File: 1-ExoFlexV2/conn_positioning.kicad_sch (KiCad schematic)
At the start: 39 parts, among them J46 POS_LC1, J47 POS_LC2, J48 POS_LC3, J49 1751099, J50 1751099, J51 1751099, J52 1751112, J53 1751112, J54 1751112, J55 200k, J56 200k, J57 200k, J58 5,1k, J59 5,1k, J60 5,1k

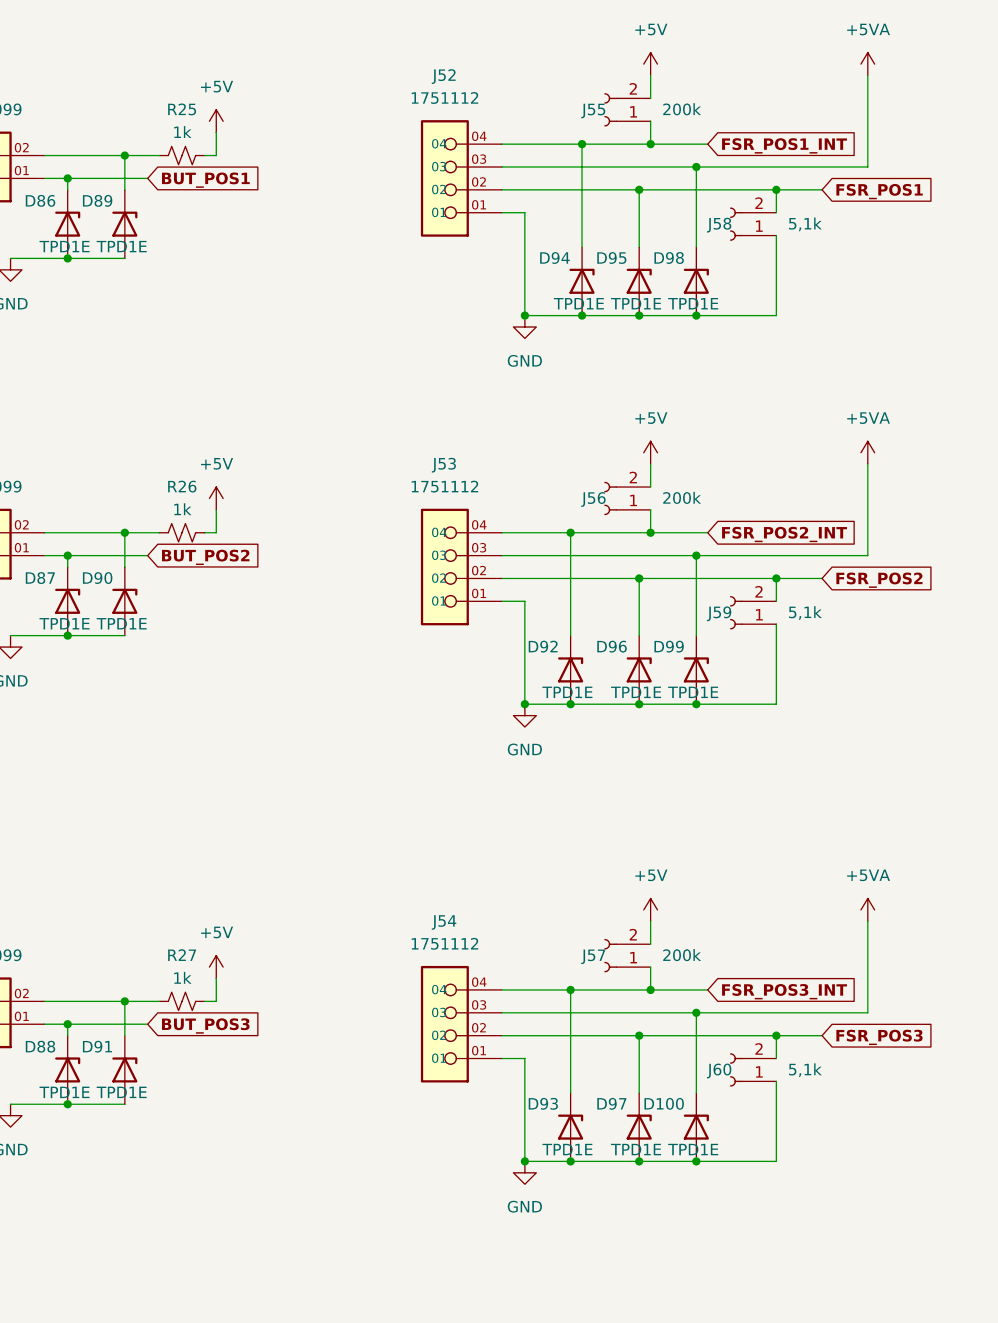
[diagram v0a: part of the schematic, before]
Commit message: Trimmer et jumper
-Changement de symbole de jumper
-Ajout des des trimmer aux endroits nécessaires
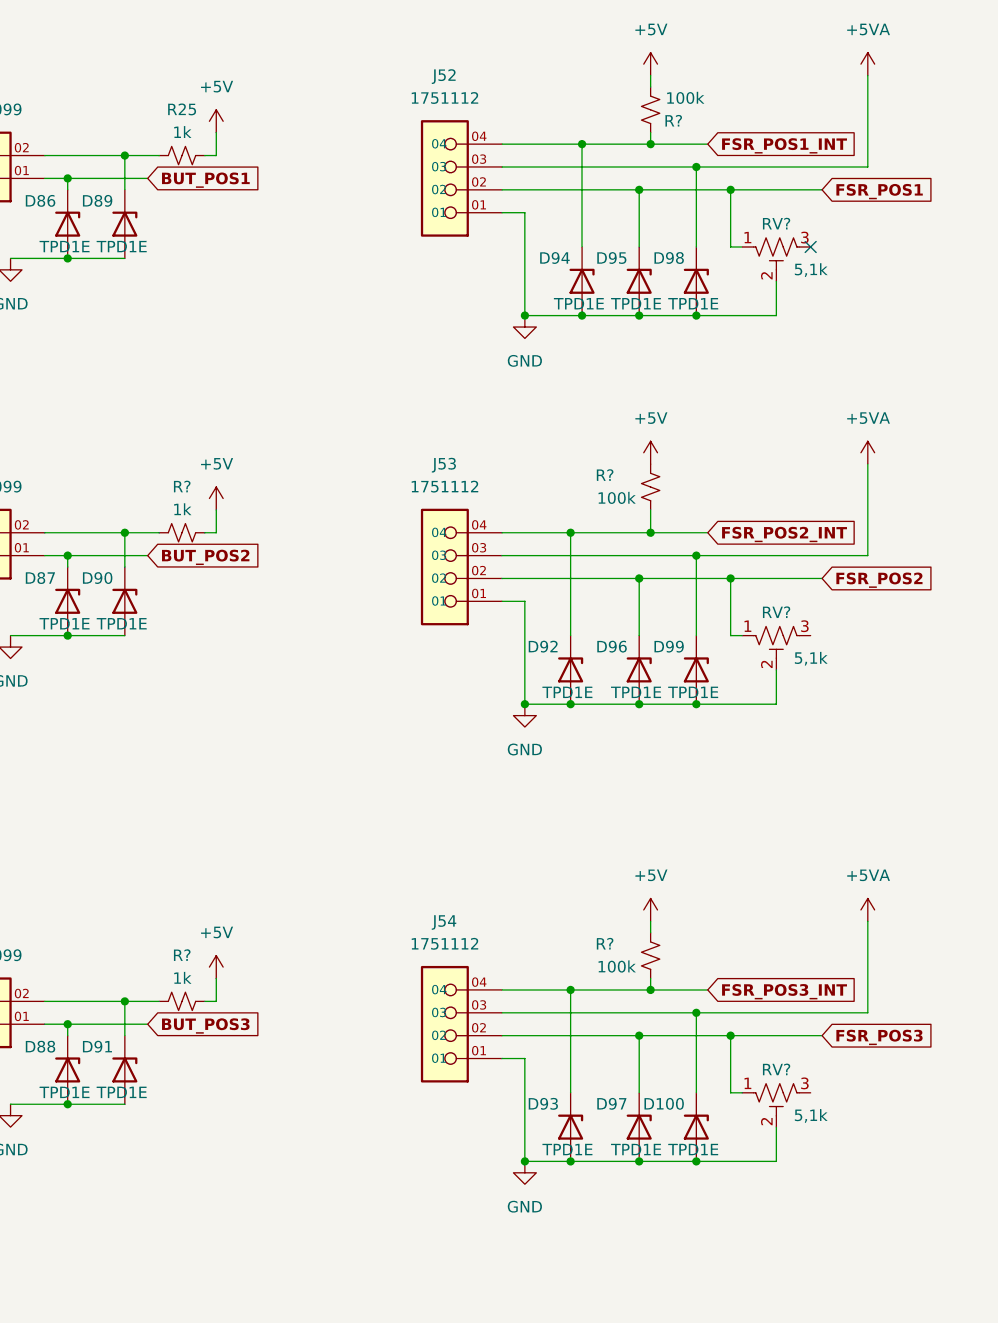
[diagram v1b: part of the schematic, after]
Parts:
- removed J55, J56, J57: 200k, Connector_PinHeader_2.54mm:PinHeader_1x02_P2.54mm_Vertical, symbol Connector:Conn_01x02_Female
- removed J58, J59, J60: 5,1k, Connector_PinHeader_2.54mm:PinHeader_1x02_P2.54mm_Vertical, symbol Connector:Conn_01x02_Female
- removed R26, R27: 1k, Resistor_SMD:R_0603_1608Metric, symbol Device:R_Small_US
- added R? (x2): 1k, Resistor_SMD:R_0805_2012Metric, symbol Device:R_Small_US
- added R? (x3): 100k, Resistor_SMD:R_0805_2012Metric, symbol Device:R_Small_US
- added RV? (x3): 5,1k, FootPrint:TRIM_3362P-1-102LF, symbol Device:R_Potentiometer_Trim_US
- R25: footprint Resistor_SMD:R_0603_1608Metric -> Resistor_SMD:R_0805_2012Metric
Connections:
- net +5V: now also R?.1, R?.1, R?.1, R?.2, R?.2
- net FSR_POS1: now also RV?.1
- net FSR_POS1_INT: now also R?.2
- net FSR_POS2: now also RV?.1
- net FSR_POS2_INT: now also R?.2
- net FSR_POS3: now also RV?.1
- net FSR_POS3_INT: now also R?.2
- net GND: now also RV?.2, RV?.2, RV?.2
- net at D91.1 (K), J51.02: now also R?.1
- net at D90.1 (K), J50.02: now also R?.1
- no-connect marks 0 -> 1

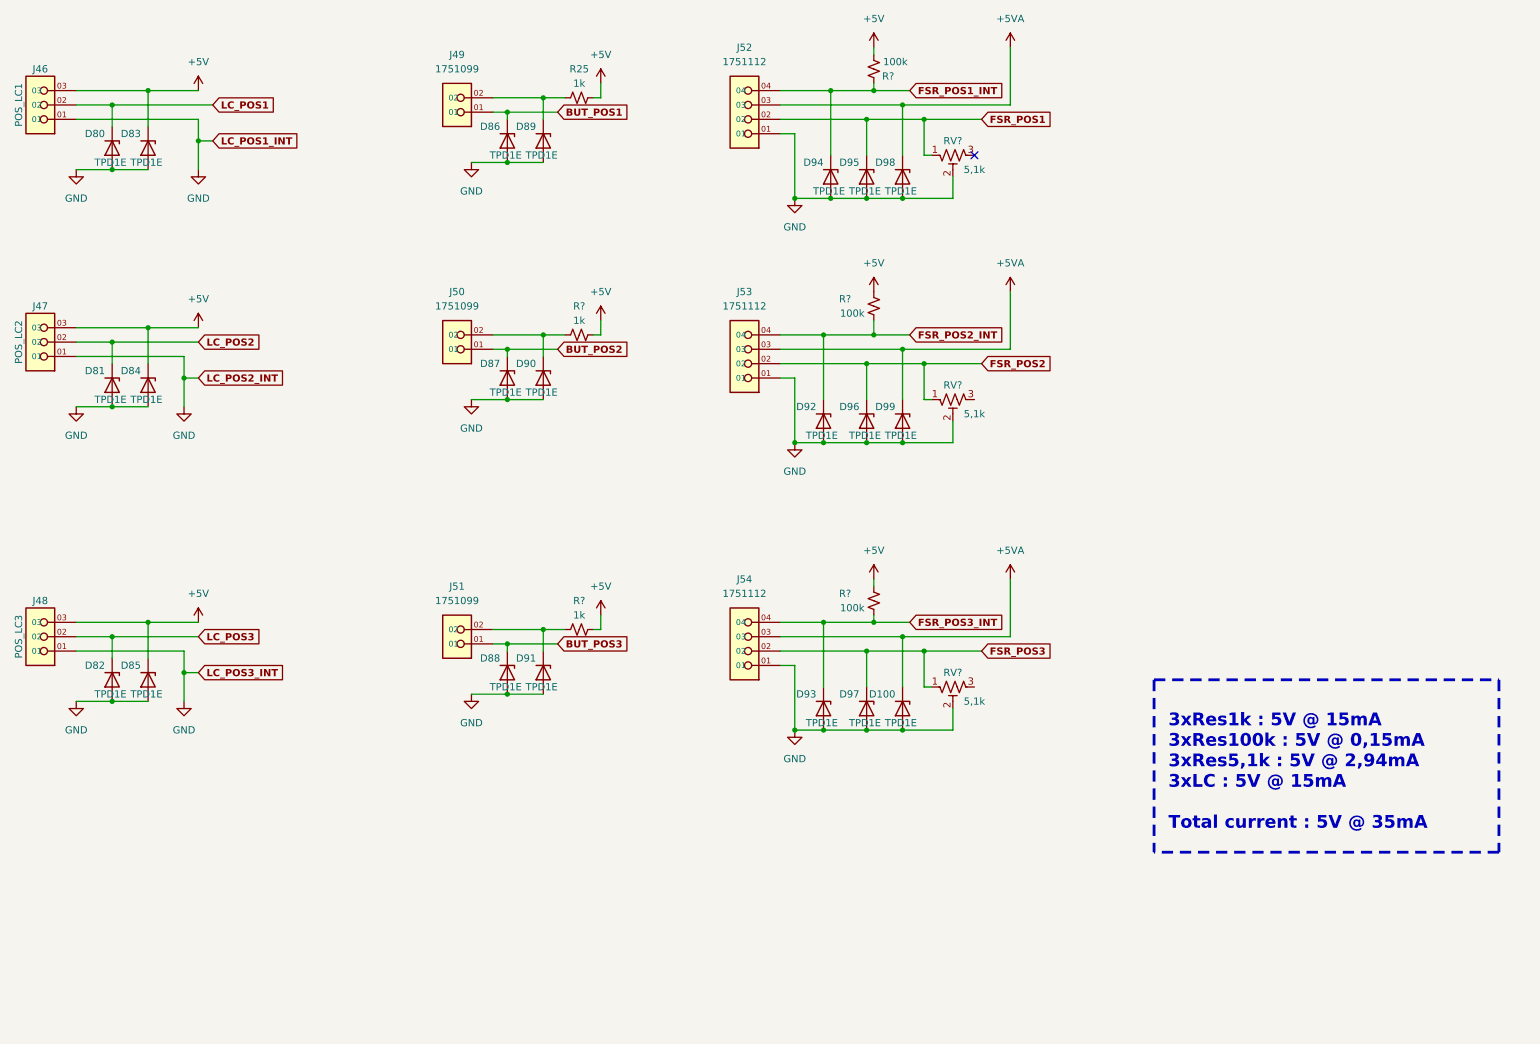
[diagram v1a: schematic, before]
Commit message: Test points et notes
- Ajout de tous les tests point nécessaires
-  Ajoute des sections de notes dans chaque page
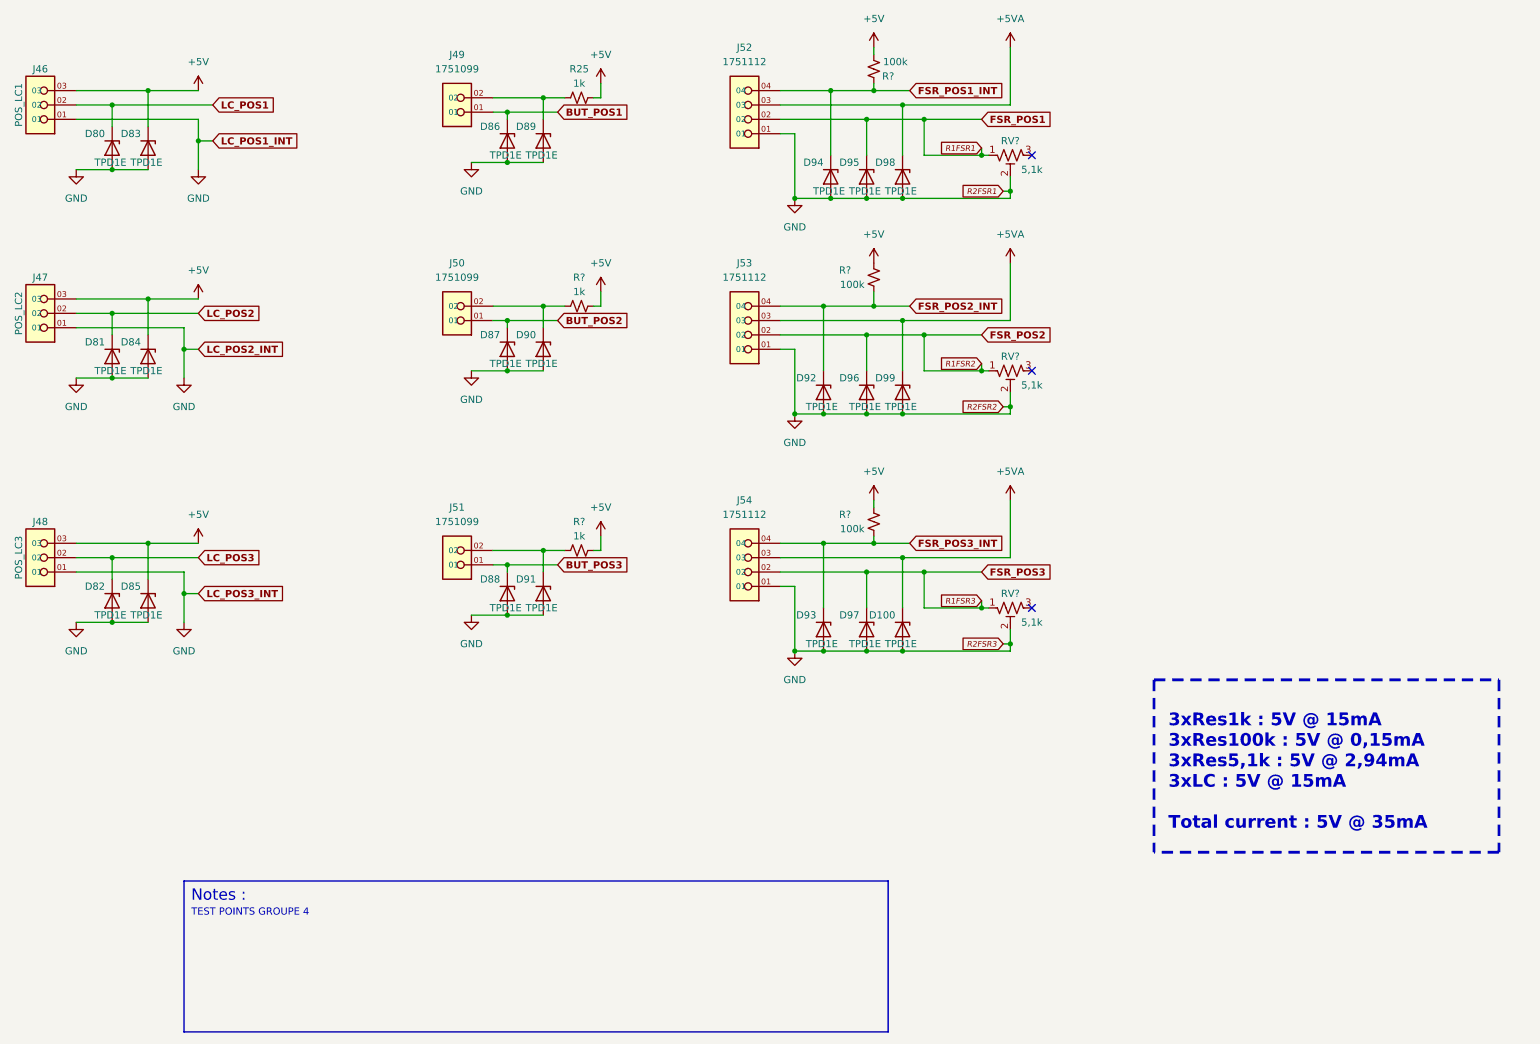
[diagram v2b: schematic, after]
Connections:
- no-connect marks 1 -> 3
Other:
- note added: "Notes :"
- note added: "TEST POINTS GROUPE 4"
- moved on the sheet: D100, D81, D82, D84, D85, D87, D88, D90, D91, D92, D93, D96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

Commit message: Schématisation terminée
- Schéma terminé
- Passage vers le PCB
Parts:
- D79: renamed from D80; value TPD1E -> TVS; DESCRIPTION (none) -> TVS DIODE 5.5VWM 14VC 2X1SON; MANUFACTURER (none) -> Texas Instruments; PACKAGE (none) -> 0402 (1006 Metric); PART NUMBER (none) -> TPD1E05U06DPYR; TYPE (none) -> SMD
- D80: renamed from D81; value TPD1E -> TVS; DESCRIPTION (none) -> TVS DIODE 5.5VWM 14VC 2X1SON; MANUFACTURER (none) -> Texas Instruments; PACKAGE (none) -> 0402 (1006 Metric); PART NUMBER (none) -> TPD1E05U06DPYR; TYPE (none) -> SMD
- D81: renamed from D82; value TPD1E -> TVS; DESCRIPTION (none) -> TVS DIODE 5.5VWM 14VC 2X1SON; MANUFACTURER (none) -> Texas Instruments; PACKAGE (none) -> 0402 (1006 Metric); PART NUMBER (none) -> TPD1E05U06DPYR; TYPE (none) -> SMD
- D82: renamed from D83; value TPD1E -> TVS; DESCRIPTION (none) -> TVS DIODE 5.5VWM 14VC 2X1SON; MANUFACTURER (none) -> Texas Instruments; PACKAGE (none) -> 0402 (1006 Metric); PART NUMBER (none) -> TPD1E05U06DPYR; TYPE (none) -> SMD
- D83: renamed from D84; value TPD1E -> TVS; DESCRIPTION (none) -> TVS DIODE 5.5VWM 14VC 2X1SON; MANUFACTURER (none) -> Texas Instruments; PACKAGE (none) -> 0402 (1006 Metric); PART NUMBER (none) -> TPD1E05U06DPYR; TYPE (none) -> SMD
- D84: renamed from D85; value TPD1E -> TVS; DESCRIPTION (none) -> TVS DIODE 5.5VWM 14VC 2X1SON; MANUFACTURER (none) -> Texas Instruments; PACKAGE (none) -> 0402 (1006 Metric); PART NUMBER (none) -> TPD1E05U06DPYR; TYPE (none) -> SMD
- D85: renamed from D86; value TPD1E -> TVS; DESCRIPTION (none) -> TVS DIODE 5.5VWM 14VC 2X1SON; MANUFACTURER (none) -> Texas Instruments; PACKAGE (none) -> 0402 (1006 Metric); PART NUMBER (none) -> TPD1E05U06DPYR; TYPE (none) -> SMD
- D86: renamed from D87; value TPD1E -> TVS; DESCRIPTION (none) -> TVS DIODE 5.5VWM 14VC 2X1SON; MANUFACTURER (none) -> Texas Instruments; PACKAGE (none) -> 0402 (1006 Metric); PART NUMBER (none) -> TPD1E05U06DPYR; TYPE (none) -> SMD
- D87: renamed from D88; value TPD1E -> TVS; DESCRIPTION (none) -> TVS DIODE 5.5VWM 14VC 2X1SON; MANUFACTURER (none) -> Texas Instruments; PACKAGE (none) -> 0402 (1006 Metric); PART NUMBER (none) -> TPD1E05U06DPYR; TYPE (none) -> SMD
- D88: renamed from D89; value TPD1E -> TVS; DESCRIPTION (none) -> TVS DIODE 5.5VWM 14VC 2X1SON; MANUFACTURER (none) -> Texas Instruments; PACKAGE (none) -> 0402 (1006 Metric); PART NUMBER (none) -> TPD1E05U06DPYR; TYPE (none) -> SMD
- D89: renamed from D90; value TPD1E -> TVS; DESCRIPTION (none) -> TVS DIODE 5.5VWM 14VC 2X1SON; MANUFACTURER (none) -> Texas Instruments; PACKAGE (none) -> 0402 (1006 Metric); PART NUMBER (none) -> TPD1E05U06DPYR; TYPE (none) -> SMD
- D90: renamed from D91; value TPD1E -> TVS; DESCRIPTION (none) -> TVS DIODE 5.5VWM 14VC 2X1SON; MANUFACTURER (none) -> Texas Instruments; PACKAGE (none) -> 0402 (1006 Metric); PART NUMBER (none) -> TPD1E05U06DPYR; TYPE (none) -> SMD
- D91: renamed from D92; value TPD1E -> TVS; DESCRIPTION (none) -> TVS DIODE 5.5VWM 14VC 2X1SON; MANUFACTURER (none) -> Texas Instruments; PACKAGE (none) -> 0402 (1006 Metric); PART NUMBER (none) -> TPD1E05U06DPYR; TYPE (none) -> SMD
- D92: renamed from D93; value TPD1E -> TVS; DESCRIPTION (none) -> TVS DIODE 5.5VWM 14VC 2X1SON; MANUFACTURER (none) -> Texas Instruments; PACKAGE (none) -> 0402 (1006 Metric); PART NUMBER (none) -> TPD1E05U06DPYR; TYPE (none) -> SMD
- D93: renamed from D94; value TPD1E -> TVS; DESCRIPTION (none) -> TVS DIODE 5.5VWM 14VC 2X1SON; MANUFACTURER (none) -> Texas Instruments; PACKAGE (none) -> 0402 (1006 Metric); PART NUMBER (none) -> TPD1E05U06DPYR; TYPE (none) -> SMD
- D94: renamed from D95; value TPD1E -> TVS; DESCRIPTION (none) -> TVS DIODE 5.5VWM 14VC 2X1SON; MANUFACTURER (none) -> Texas Instruments; PACKAGE (none) -> 0402 (1006 Metric); PART NUMBER (none) -> TPD1E05U06DPYR; TYPE (none) -> SMD
- D95: renamed from D96; value TPD1E -> TVS; DESCRIPTION (none) -> TVS DIODE 5.5VWM 14VC 2X1SON; MANUFACTURER (none) -> Texas Instruments; PACKAGE (none) -> 0402 (1006 Metric); PART NUMBER (none) -> TPD1E05U06DPYR; TYPE (none) -> SMD
- D96: renamed from D97; value TPD1E -> TVS; DESCRIPTION (none) -> TVS DIODE 5.5VWM 14VC 2X1SON; MANUFACTURER (none) -> Texas Instruments; PACKAGE (none) -> 0402 (1006 Metric); PART NUMBER (none) -> TPD1E05U06DPYR; TYPE (none) -> SMD
- D97: renamed from D98; value TPD1E -> TVS; DESCRIPTION (none) -> TVS DIODE 5.5VWM 14VC 2X1SON; MANUFACTURER (none) -> Texas Instruments; PACKAGE (none) -> 0402 (1006 Metric); PART NUMBER (none) -> TPD1E05U06DPYR; TYPE (none) -> SMD
- D98: renamed from D99; value TPD1E -> TVS; DESCRIPTION (none) -> TVS DIODE 5.5VWM 14VC 2X1SON; MANUFACTURER (none) -> Texas Instruments; PACKAGE (none) -> 0402 (1006 Metric); PART NUMBER (none) -> TPD1E05U06DPYR; TYPE (none) -> SMD
- D99: renamed from D100; value TPD1E -> TVS; DESCRIPTION (none) -> TVS DIODE 5.5VWM 14VC 2X1SON; MANUFACTURER (none) -> Texas Instruments; PACKAGE (none) -> 0402 (1006 Metric); PART NUMBER (none) -> TPD1E05U06DPYR; TYPE (none) -> SMD
- J47: renamed from J46; value POS_LC1 -> 3; DESCRIPTION (none) -> 3 Position Wire to Board Terminal Block 55° (125°) Angle wi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; PACKAGE (none) -> 3 POS 0.100" (2.54mm); PART NUMBER (none) -> 1751109; TYPE (none) -> Through Hole
- J48: renamed from J47; value POS_LC2 -> 3; DESCRIPTION (none) -> 3 Position Wire to Board Terminal Block 55° (125°) Angle wi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; PACKAGE (none) -> 3 POS 0.100" (2.54mm); PART NUMBER (none) -> 1751109; TYPE (none) -> Through Hole
- J49: renamed from J48; value POS_LC3 -> 3; DESCRIPTION (none) -> 3 Position Wire to Board Terminal Block 55° (125°) Angle wi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; PACKAGE (none) -> 3 POS 0.100" (2.54mm); PART NUMBER (none) -> 1751109; TYPE (none) -> Through Hole
- J50: renamed from J49; value 1751099 -> 2; DESCRIPTION (none) -> 2 Position Wire to Board Terminal Block 55° (125°) Angle wi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; PACKAGE (none) -> 2 POS 0.100" (2.54mm); PART NUMBER (none) -> 1751099; TYPE (none) -> Through Hole
- J51: renamed from J50; value 1751099 -> 2; DESCRIPTION (none) -> 2 Position Wire to Board Terminal Block 55° (125°) Angle wi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; PACKAGE (none) -> 2 POS 0.100" (2.54mm); PART NUMBER (none) -> 1751099; TYPE (none) -> Through Hole
- J52: renamed from J51; value 1751099 -> 2; DESCRIPTION (none) -> 2 Position Wire to Board Terminal Block 55° (125°) Angle wi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; PACKAGE (none) -> 2 POS 0.100" (2.54mm); PART NUMBER (none) -> 1751099; TYPE (none) -> Through Hole
- J53: renamed from J52; value 1751112 -> 4; DESCRIPTION (none) -> 4 Position Wire to Board Terminal Block 55° (125°) Angle wi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; PACKAGE (none) -> 4 POS 0.100" (2.54mm); PART NUMBER (none) -> 1751112; TYPE (none) -> Through Hole
- J54: renamed from J53; value 1751112 -> 4; DESCRIPTION (none) -> 4 Position Wire to Board Terminal Block 55° (125°) Angle wi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; PACKAGE (none) -> 4 POS 0.100" (2.54mm); PART NUMBER (none) -> 1751112; TYPE (none) -> Through Hole
- J55: renamed from J54; value 1751112 -> 4; DESCRIPTION (none) -> 4 Position Wire to Board Terminal Block 55° (125°) Angle wi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; PACKAGE (none) -> 4 POS 0.100" (2.54mm); PART NUMBER (none) -> 1751112; TYPE (none) -> Through Hole
- R29: renamed from R25; value 1k -> 1k 1% 1/10W; footprint Resistor_SMD:R_0805_2012Metric -> Resistor_SMD:R_0402_1005Metric; DESCRIPTION (none) -> 1 kOhms ±1% 0.1W, 1/10W Chip Resistor 0402 (1005 Metric) Au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; MANUFACTURER (none) -> Panasonic Electronic Components; PACKAGE (none) -> 0402 (1005 Metric); PART NUMBER (none) -> ERJ-2RKF1001X; TYPE (none) -> SMD
- R30, R31: renamed from R?; value 1k -> 1k 1% 1/10W; footprint Resistor_SMD:R_0805_2012Metric -> Resistor_SMD:R_0402_1005Metric; DESCRIPTION (none) -> 1 kOhms ±1% 0.1W, 1/10W Chip Resistor 0402 (1005 Metric) Au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; MANUFACTURER (none) -> Panasonic Electronic Components; PACKAGE (none) -> 0402 (1005 Metric); PART NUMBER (none) -> ERJ-2RKF1001X; TYPE (none) -> SMD
- R32, R33, R34: renamed from R?; value 100k -> 100k 5% 1/8W; DESCRIPTION (none) -> 100 kOhms ±5% 0.125W, 1/8W Chip Resistor 0805 (2012 Metric)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; MANUFACTURER (none) -> Panasonic Electronic Components; PACKAGE (none) -> 0805 (2012 Metric); PART NUMBER (none) -> ERJ-6GEYJ104V; TYPE (none) -> SMD
- RV6, RV7, RV8: renamed from RV?; value 5,1k -> Trim 10k; footprint FootPrint:TRIM_3362P-1-102LF -> FootPrint:TRIM_3362P-1-103LF; DESCRIPTION (none) -> Trimmer 10k 0,5W PC PIN TOP; MANUFACTURER (none) -> Bourns Inc.; PACKAGE (none) -> Rectangular - 0.275" x 0.260" Face; PART NUMBER (none) -> 3362P-1-103LF; TYPE (none) -> Through Hole
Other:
- note added: "3xRes1k : 5V @ 15mA 3xRes100k : 5V @ 0,15mA 3xRes5,1k : 5V @ 10mA 3xLC : 5V @ 15mA Total current : 5V @ 45mA"
- note added: "5,1kΩ"
- note added: "But Pos 1"
- note added: "But Pos 2"
- note added: "But Pos 3"
- note added: "FSR 1"
- note added: "FSR 2"
- note added: "FSR 3"
- note added: "LC Pos 1"
- note added: "LC Pos 2"
- note added: "LC Pos 3"
- note removed: "3xRes1k : 5V @ 15mA 3xRes100k : 5V @ 0,15mA 3xRes5,1k : 5V @ 2,94mA 3xLC : 5V @ 15mA Total current : 5V @ 35mA"
